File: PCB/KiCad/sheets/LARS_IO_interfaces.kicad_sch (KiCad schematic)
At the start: 52 parts, among them J10 I2C1, J11 I2C1, J12 Servo 1, J13 Servo 2, J14 TIM1, J15 TIM2, J16 I2C2, J17 I2C2, J18 I2C2, J19 I2C2, J20 Analog 1, J21 Analog 2, J22 UART1, J23 UART2, J24 UART3, J25 3.3V Out, J26 GPIO, J31 5V Out, J4 CAN1, J5 CAN1, J6 SPI1, J7 SPI1, J8 I2C1, J9 I2C1

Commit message: reannotate schematic
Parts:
- renumbered C49 to C47, C50 to C48, C56 to C49, C70 to C50, C53 to C51, C54 to C52, C55 to C53, C47 to C54, C48 to C55, C62 to C56, C69 to C57, C57 to C58, C51 to C59, C52 to C60, J14 to J12, J15 to J13, J16 to J14, J17 to J15, J18 to J16, J19 to J17, J25 to J18, J31 to J19, J22 to J20, J23 to J21, J24 to J22, J12 to J23, J13 to J24, J26 to J25, J20 to J26, J21 to J27
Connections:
- net CAN1_HIGH renamed CAN1_P
- net CAN1_LOW renamed CAN1_N

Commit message: add final traces
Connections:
- net SPI1_MISO: now also J6.4 (Pin_4), J7.4 (Pin_4); no longer J6.3 (Pin_3), J7.3 (Pin_3)
- net SPI1_MOSI: now also J6.5 (Pin_5), J7.5 (Pin_5); no longer J6.4 (Pin_4), J7.4 (Pin_4)
- net SPI1_SCLK: now also J6.3 (Pin_3), J7.3 (Pin_3); no longer J6.5 (Pin_5), J7.5 (Pin_5)

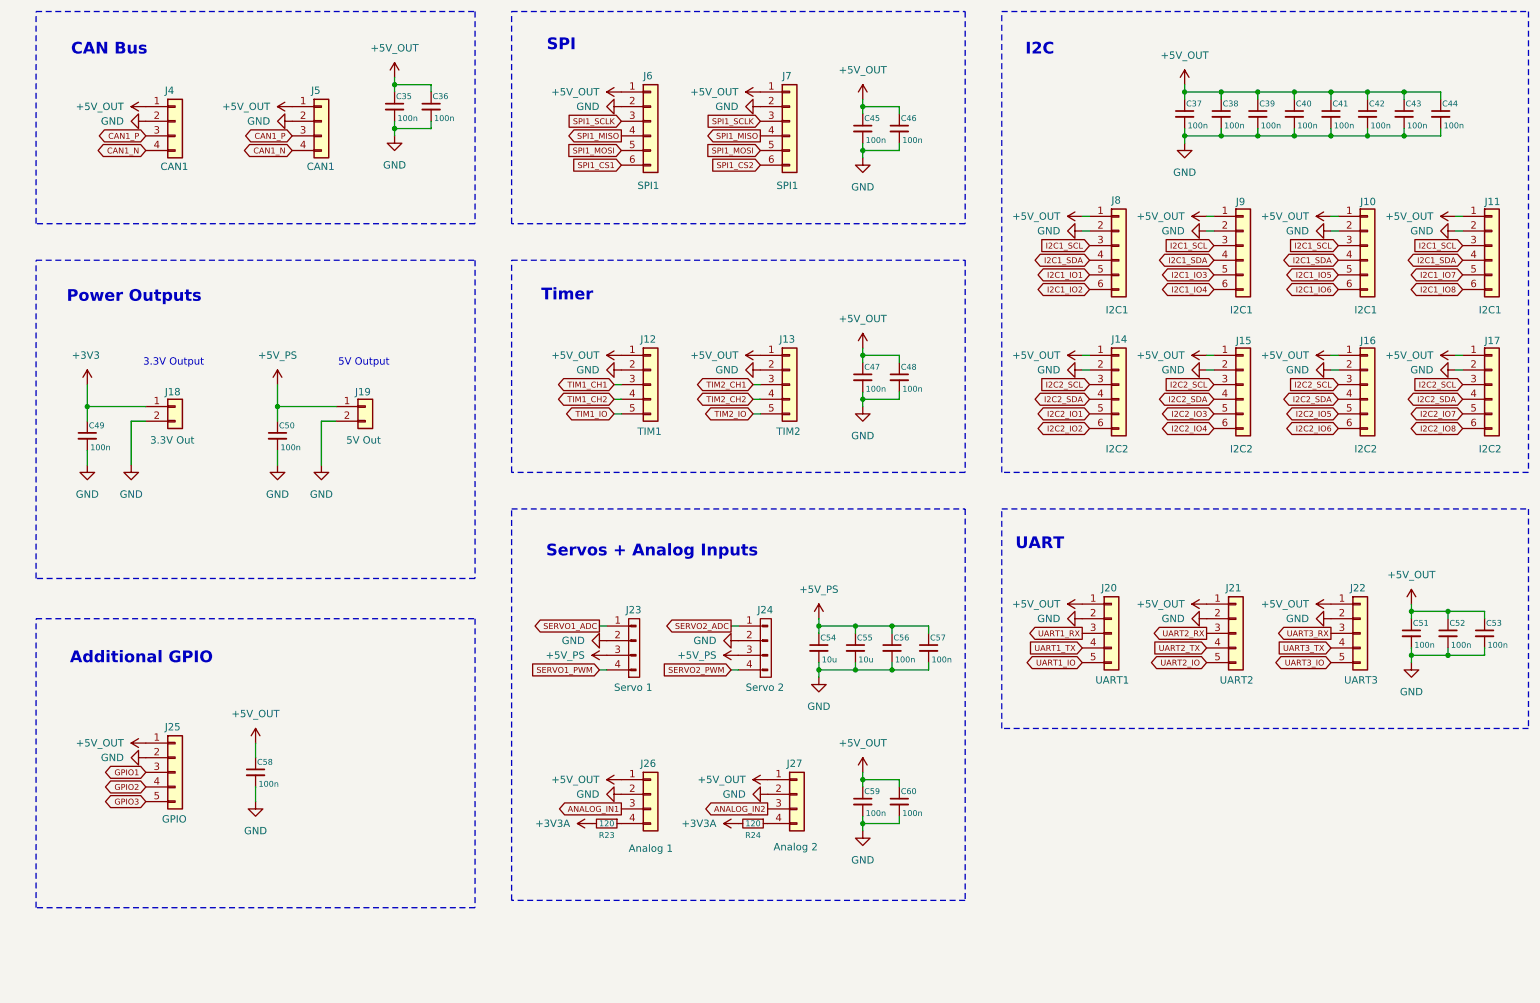
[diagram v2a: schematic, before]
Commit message: change default KiCad schematic font
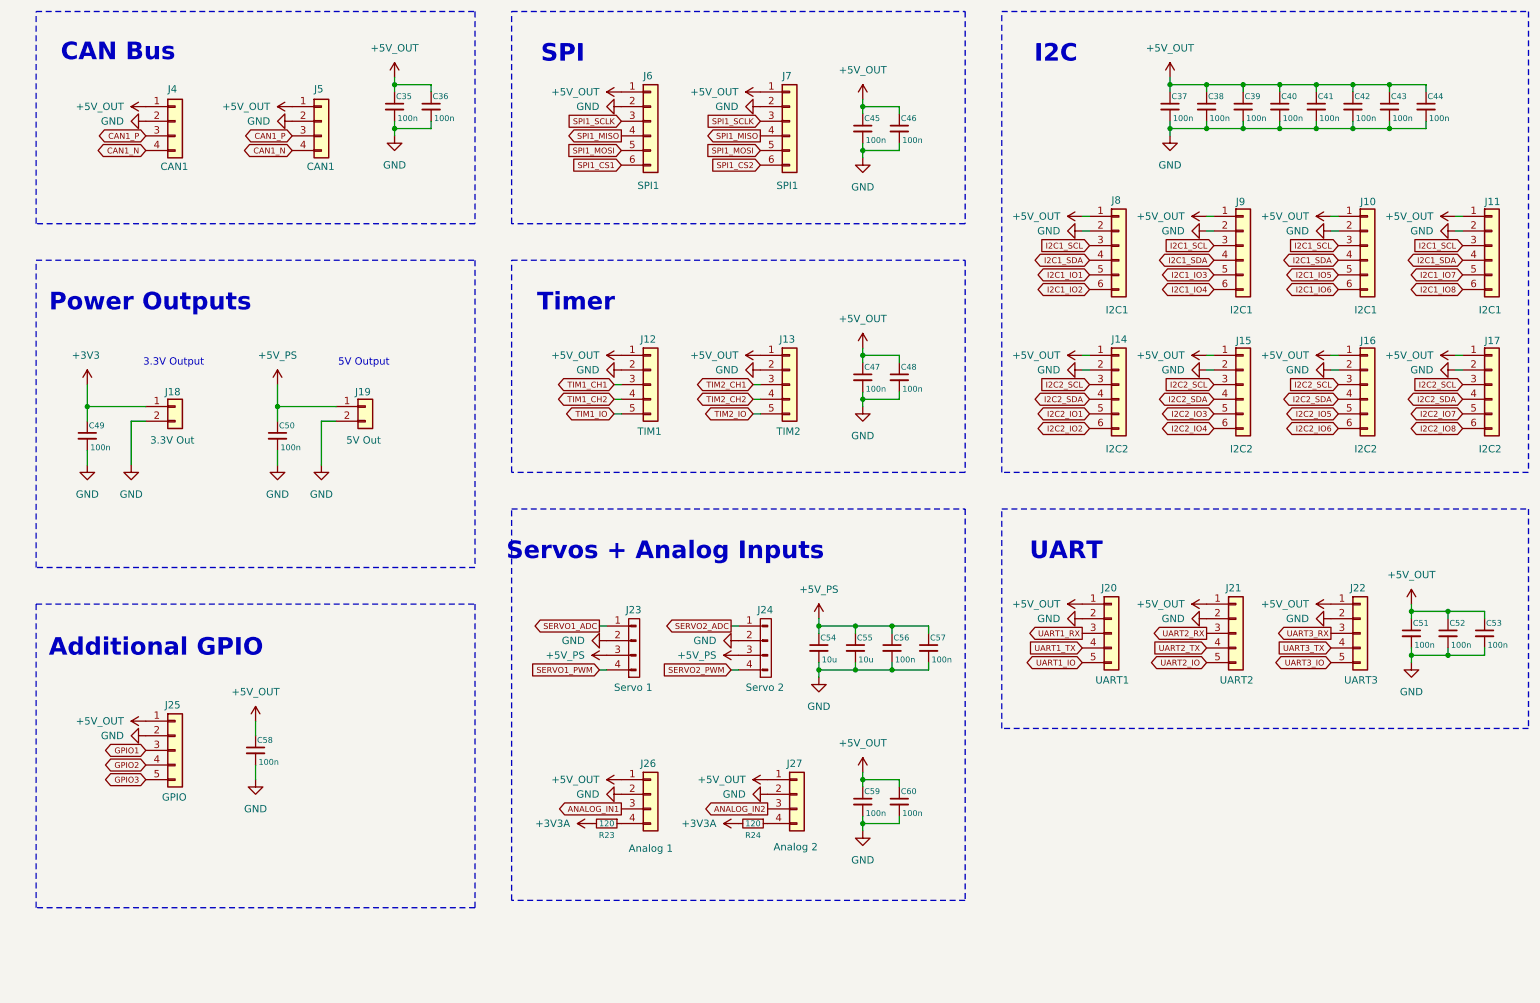
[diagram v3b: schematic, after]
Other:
- moved on the sheet: C37, C38, C39, C40, C41, C42, C43, C44, C58, J25

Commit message: update text layout and fix remaining DRC errors
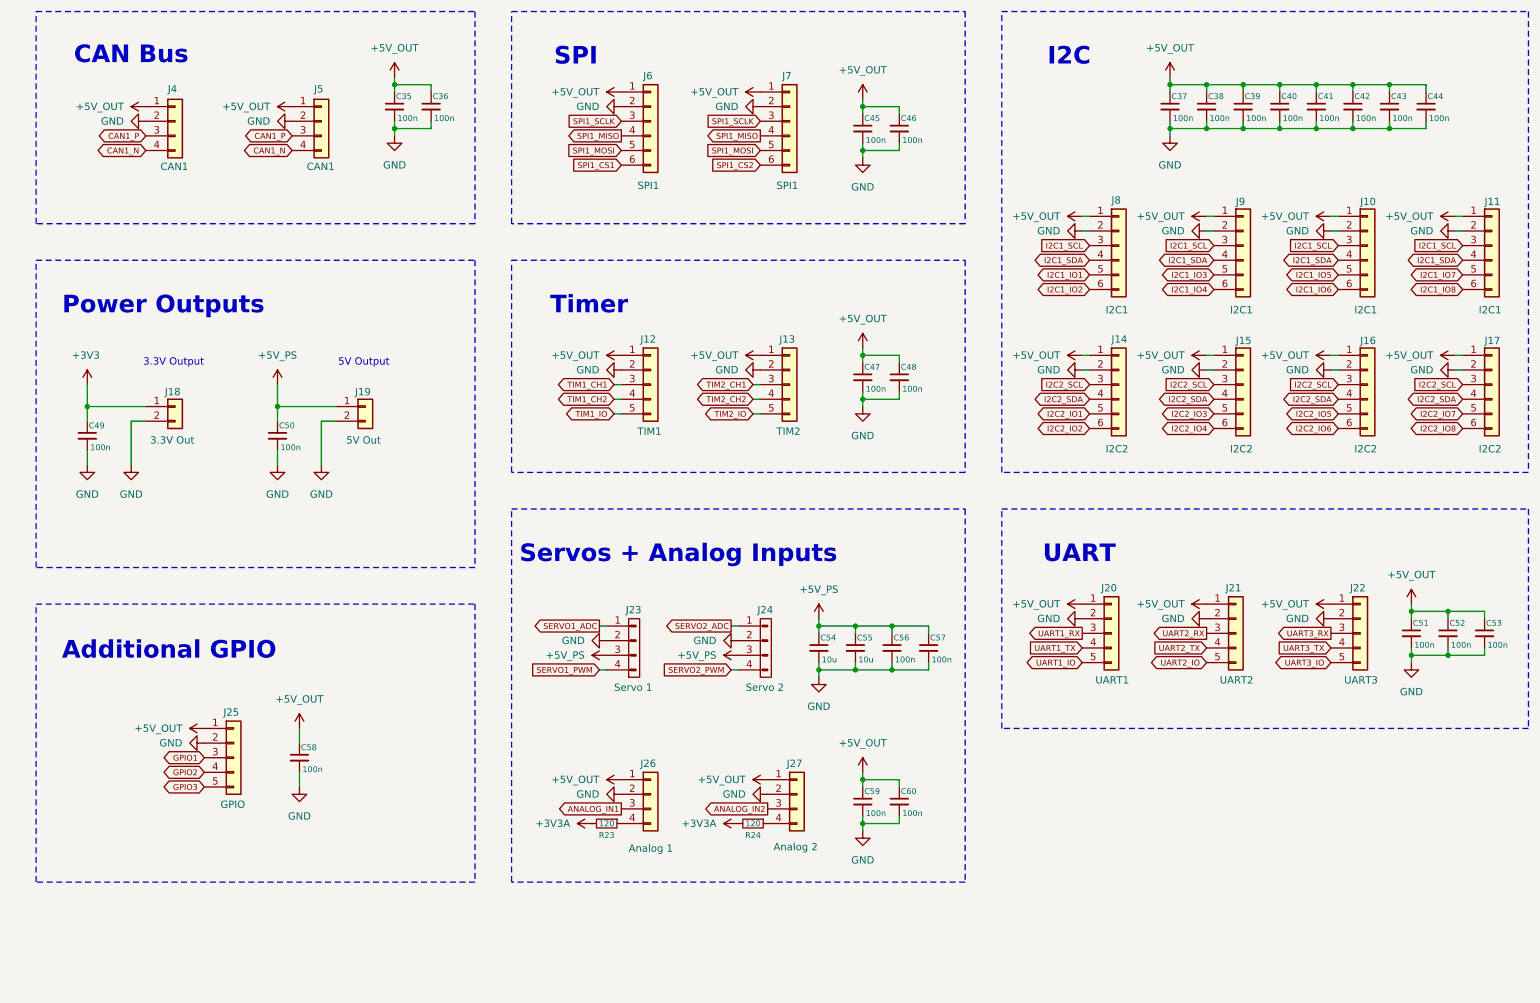
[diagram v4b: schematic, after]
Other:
- moved on the sheet: C58, J25
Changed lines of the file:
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@@
 	(rectangle
 		(start 101.6 105.41)
-		(end 180.34 173.355)
+		(end 180.34 170.18)
 		(stroke
 			(width 0)
@@
 	(rectangle
 		(start 19.05 121.92)
-		(end 95.25 174.625)
+		(end 95.25 170.18)
 		(stroke
 			(width 0)
@@
 	(text "Servos + Analog Inputs\n"
 		(exclude_from_sim no)
-		(at 128.27 112.776 0)
+		(at 130.556 113.284 0)
 		(effects
 			(font
@@
 	(text "CAN Bus"
 		(exclude_from_sim no)
-		(at 33.274 26.162 0)
+		(at 35.56 26.67 0)
 		(effects
 			(font
@@
 	(text "Timer"
 		(exclude_from_sim no)
-		(at 112.776 69.596 0)
+		(at 115.062 70.104 0)
 		(effects
 			(font
@@
 	(text "Power Outputs"
 		(exclude_from_sim no)
-		(at 38.862 69.596 0)
+		(at 41.148 70.104 0)
 		(effects
 			(font
@@
 	(text "SPI"
 		(exclude_from_sim no)
-		(at 110.49 26.416 0)
+		(at 112.776 26.924 0)
 		(effects
 			(font
@@
 	(text "UART\n"
 		(exclude_from_sim no)
-		(at 197.866 112.776 0)
+		(at 200.152 113.284 0)
 		(effects
 			(font
@@
 	(text "I2C"
 		(exclude_from_sim no)
-		(at 196.088 26.416 0)
+		(at 198.374 26.924 0)
 		(effects
 			(font
@@
 	(text "Additional GPIO"
 		(exclude_from_sim no)
-		(at 39.878 129.54 0)
+		(at 42.164 130.048 0)
 		(effects
 			(font
@@
 	(wire
 		(pts
-			(xy 57.15 149.86) (xy 57.15 152.4)
+			(xy 64.77 151.13) (xy 64.77 153.67)
 		)
 		(stroke
@@
 	(wire
 		(pts
-			(xy 57.15 142.24) (xy 57.15 144.78)
+			(xy 64.77 143.51) (xy 64.77 146.05)
 		)
 		(stroke
@@
 	(global_label "GPIO1"
 		(shape bidirectional)
-		(at 38.1 147.32 180)
+		(at 48.26 148.59 180)
 		(fields_autoplaced yes)
 		(effects
@@
 		)
 		(property "Intersheetrefs" "${INTERSHEET_REFS}"
-			(at 30.2753 147.32 0)
+			(at 40.4353 148.59 0)
 			(effects
 				(font
@@
 	(global_label "GPIO3"
 		(shape bidirectional)
-		(at 38.1 152.4 180)
+		(at 48.26 153.67 180)
 		(fields_autoplaced yes)
 		(effects
@@
 		)
 		(property "Intersheetrefs" "${INTERSHEET_REFS}"
-			(at 30.2753 152.4 0)
+			(at 40.4353 153.67 0)
 			(effects
 				(font
@@
 	(global_label "GPIO2"
 		(shape bidirectional)
-		(at 38.1 149.86 180)
+		(at 48.26 151.13 180)
 		(fields_autoplaced yes)
 		(effects
@@
 		)
 		(property "Intersheetrefs" "${INTERSHEET_REFS}"
-			(at 30.2753 149.86 0)
+			(at 40.4353 151.13 0)
 			(effects
 				(font
@@
 	(symbol
 		(lib_id "power:+5V")
-		(at 38.1 142.24 90)
+		(at 48.26 143.51 90)
 		(unit 1)
 		(exclude_from_sim no)
@@
 		(fields_autoplaced yes)
 		(property "Reference" "#PWR0125"
-			(at 41.91 142.24 0)
+			(at 52.07 143.51 0)
 			(effects
 				(font
@@
 		)
 		(property "Value" "+5V_OUT"
-			(at 34.29 142.2399 90)
+			(at 44.45 143.5099 90)
 			(effects
 				(font
@@
 		)
 		(property "Footprint" ""
-			(at 38.1 142.24 0)
+			(at 48.26 143.51 0)
 			(effects
 				(font
@@
 		)
 		(property "Datasheet" ""
-			(at 38.1 142.24 0)
+			(at 48.26 143.51 0)
 			(effects
 				(font
@@
 		)
 		(property "Description" "Power symbol creates a global label with name \"+5V\""
-			(at 38.1 142.24 0)
+			(at 48.26 143.51 0)
 			(effects
 				(font
@@
 	(symbol
 		(lib_id "power:+3.3V")
-		(at 57.15 142.24 0)
+		(at 64.77 143.51 0)
 		(unit 1)
 		(exclude_from_sim no)
@@
 		(fields_autoplaced yes)
 		(property "Reference" "#PWR0126"
-			(at 57.15 146.05 0)
+			(at 64.77 147.32 0)
 			(effects
 				(font
@@
 		)
 		(property "Value" "+5V_OUT"
-			(at 57.15 137.16 0)
+			(at 64.77 138.43 0)
 			(effects
 				(font
@@
 		)
 		(property "Footprint" ""
-			(at 57.15 142.24 0)
+			(at 64.77 143.51 0)
 			(effects
 				(font
@@
 		)
 		(property "Datasheet" ""
-			(at 57.15 142.24 0)
+			(at 64.77 143.51 0)
 			(effects
 				(font
@@
 		)
 		(property "Description" "Power symbol creates a global label with name \"+3.3V\""
-			(at 57.15 142.24 0)
+			(at 64.77 143.51 0)
 			(effects
 				(font
@@
 	(symbol
 		(lib_id "power:GND")
-		(at 38.1 144.78 270)
+		(at 48.26 146.05 270)
 		(unit 1)
 		(exclude_from_sim no)
@@
 		(fields_autoplaced yes)
 		(property "Reference" "#PWR0127"
-			(at 31.75 144.78 0)
+			(at 41.91 146.05 0)
 			(effects
 				(font
@@
 		)
 		(property "Value" "GND"
-			(at 34.29 144.7799 90)
+			(at 44.45 146.0499 90)
 			(effects
 				(font
@@
 		)
 		(property "Footprint" ""
-			(at 38.1 144.78 0)
+			(at 48.26 146.05 0)
 			(effects
 				(font
@@
 		)
 		(property "Datasheet" ""
-			(at 38.1 144.78 0)
+			(at 48.26 146.05 0)
 			(effects
 				(font
@@
 		)
 		(property "Description" "Power symbol creates a global label with name \"GND\" , ground"
-			(at 38.1 144.78 0)
+			(at 48.26 146.05 0)
 			(effects
 				(font
@@
 	(symbol
 		(lib_id "power:GND")
-		(at 57.15 152.4 0)
+		(at 64.77 153.67 0)
 		(unit 1)
 		(exclude_from_sim no)
@@
 		(fields_autoplaced yes)
 		(property "Reference" "#PWR0133"
-			(at 57.15 158.75 0)
+			(at 64.77 160.02 0)
 			(effects
 				(font
@@
 		)
 		(property "Value" "GND"
-			(at 57.15 157.48 0)
+			(at 64.77 158.75 0)
 			(effects
 				(font
@@
 		)
 		(property "Footprint" ""
-			(at 57.15 152.4 0)
+			(at 64.77 153.67 0)
 			(effects
 				(font
@@
 		)
 		(property "Datasheet" ""
-			(at 57.15 152.4 0)
+			(at 64.77 153.67 0)
 			(effects
 				(font
@@
 		)
 		(property "Description" "Power symbol creates a global label with name \"GND\" , ground"
-			(at 57.15 152.4 0)
+			(at 64.77 153.67 0)
 			(effects
 				(font
@@
 	(symbol
 		(lib_id "LARS_Hardware_Interface:Connector 1x5")
-		(at 43.18 147.32 0)
+		(at 53.34 148.59 0)
 		(unit 1)
 		(exclude_from_sim no)
@@
 		(dnp no)
 		(property "Reference" "J25"
-			(at 41.402 139.446 0)
+			(at 51.562 140.716 0)
 			(effects
 				(font
@@
 		)
 		(property "Value" "GPIO"
-			(at 40.894 155.448 0)
+			(at 51.054 156.718 0)
 			(effects
 				(font
@@
 		)
 		(property "Footprint" "LARS_Hardware_Interface:JST_XH_B5B-XH-A_1x05_P2.50mm_Vertical"
-			(at 43.18 147.32 0)
+			(at 53.34 148.59 0)
 			(effects
 				(font
@@
 		)
 		(property "Datasheet" "~"
-			(at 43.18 147.32 0)
+			(at 53.34 148.59 0)
 			(effects
 				(font
@@
 		)
 		(property "Description" "Generic Connector 5-Pin (JST-XH 2.50mm)"
-			(at 43.18 147.32 0)
+			(at 53.34 148.59 0)
 			(effects
 				(font
@@
 	(symbol
 		(lib_id "LARS_Hardware_Interface:C_Small")
-		(at 57.15 147.32 0)
+		(at 64.77 148.59 0)
 		(unit 1)
 		(exclude_from_sim no)
@@
 		(dnp no)
 		(property "Reference" "C58"
-			(at 57.404 145.542 0)
+			(at 65.024 146.812 0)
 			(effects
 				(font
@@
 		)
 		(property "Value" "100n"
-			(at 57.658 149.352 0)
+			(at 65.278 150.622 0)
 			(effects
 				(font
@@
 		)
 		(property "Footprint" "LARS_Hardware_Interface:C_0805_2012Metric"
-			(at 57.15 147.32 0)
+			(at 64.77 148.59 0)
 			(effects
 				(font
@@
 		)
 		(property "Datasheet" "~"
-			(at 57.15 147.32 0)
+			(at 64.77 148.59 0)
 			(effects
 				(font
@@
 		)
 		(property "Description" "Unpolarized capacitor, small symbol"
-			(at 57.15 147.32 0)
+			(at 64.77 148.59 0)
 			(effects
 				(font
